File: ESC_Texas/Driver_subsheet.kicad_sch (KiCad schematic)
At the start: 25 parts, among them IC1 UCC21331CQDRQ1, Q1 IPD100N06S4, Q2 IPD100N06S4

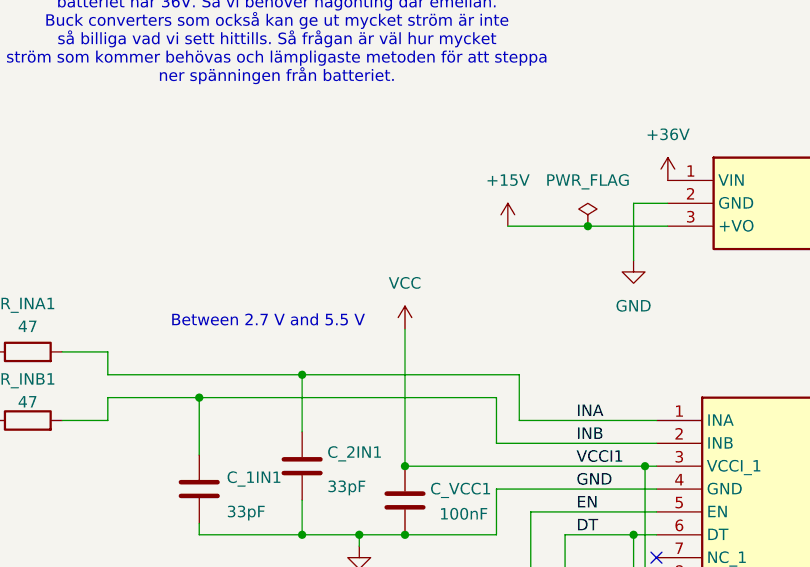
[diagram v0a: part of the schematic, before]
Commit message: Added pin connections
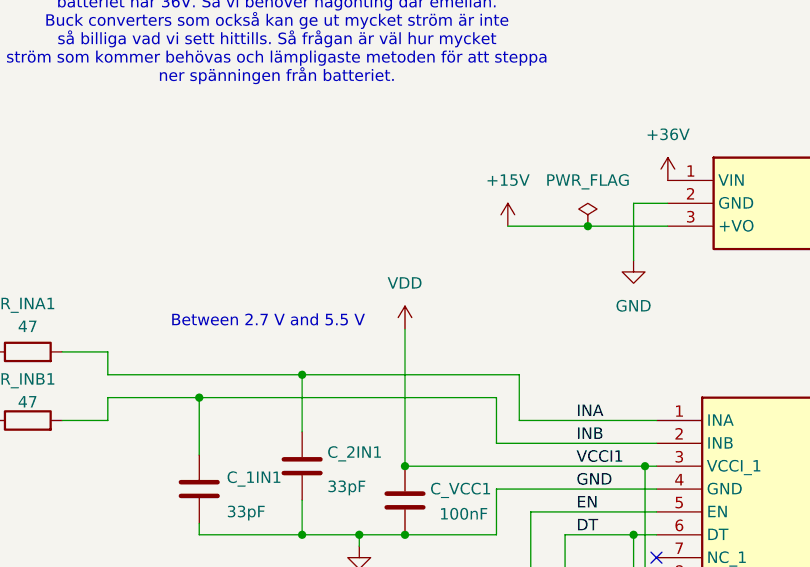
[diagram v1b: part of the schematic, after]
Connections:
- net VCC renamed VDD
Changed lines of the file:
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@@
 			)
 		)
-		(property "Value" "VCC"
+		(property "Value" "VDD"
 			(at 100.33 71.12 0)
 			(effects

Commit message: Started PCB layouting
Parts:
- C_BOOT_A1: value C -> 1uF
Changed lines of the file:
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@@
 			)
 		)
-		(property "Value" "C"
+		(property "Value" "1uF"
 			(at 184.15 96.5199 0)
 			(effects

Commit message: Layout done
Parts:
- removed PS1: MP-K78U15-500R3L, MP-K78U15-500R3L:MPK78U15500R3L, symbol MP-K78U15-500R3L:MP-K78U15-500R3L
- renumbered C_1IN1 to C_1IN2, C_2IN1 to C_2IN2, C_3IN1 to C_3IN2, C_BOOT_A1 to C_BOOT_A2, C_DT1 to C_DT2, C_EN1 to C_EN2, C_VCC1 to C_VCC2, C_VDD_B1 to C_VDD_B2, D1 to D4, D2 to D5, D3 to D6, IC1 to IC7, Q1 to Q3, Q2 to Q4, RR_ON_B1 to RR_ON_B2, R_BOOT_A1 to R_BOOT_A2, R_DT1 to R_DT2, R_GS_A1 to R_GS_A2, R_GS_B1 to R_GS_B2, R_INA1 to R_INA2, R_INB1 to R_INB2, R_OFF_A1 to R_OFF_A2, R_OFF_B1 to R_OFF_B2, R_ON_A1 to R_ON_A2

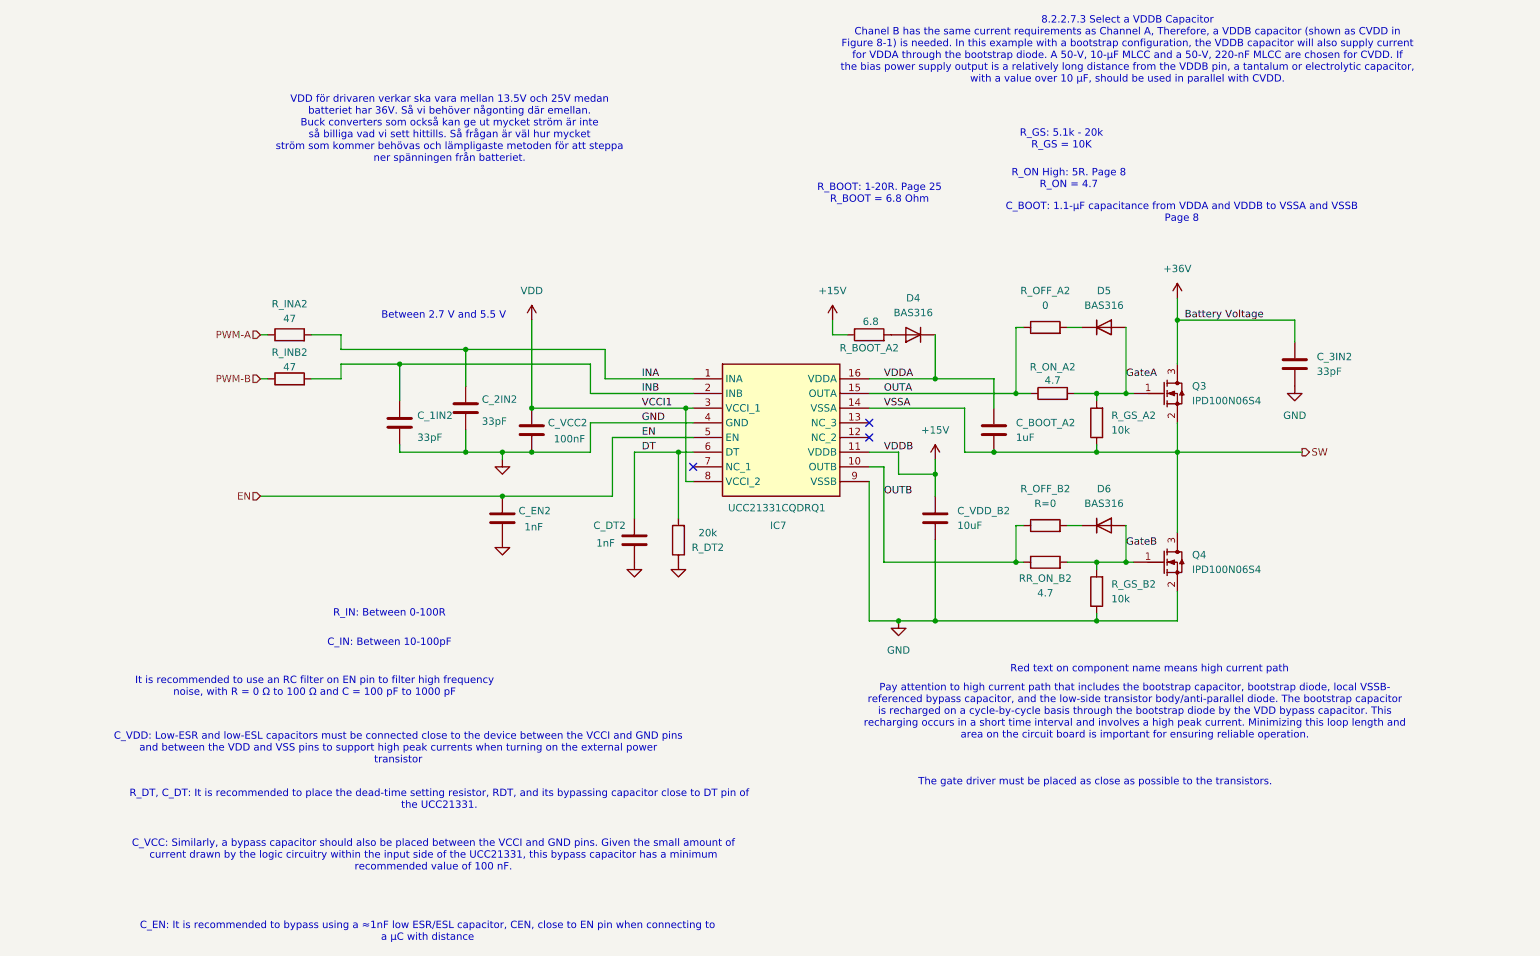
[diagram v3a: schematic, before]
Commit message: Added bypass capacitors to dc/dc...
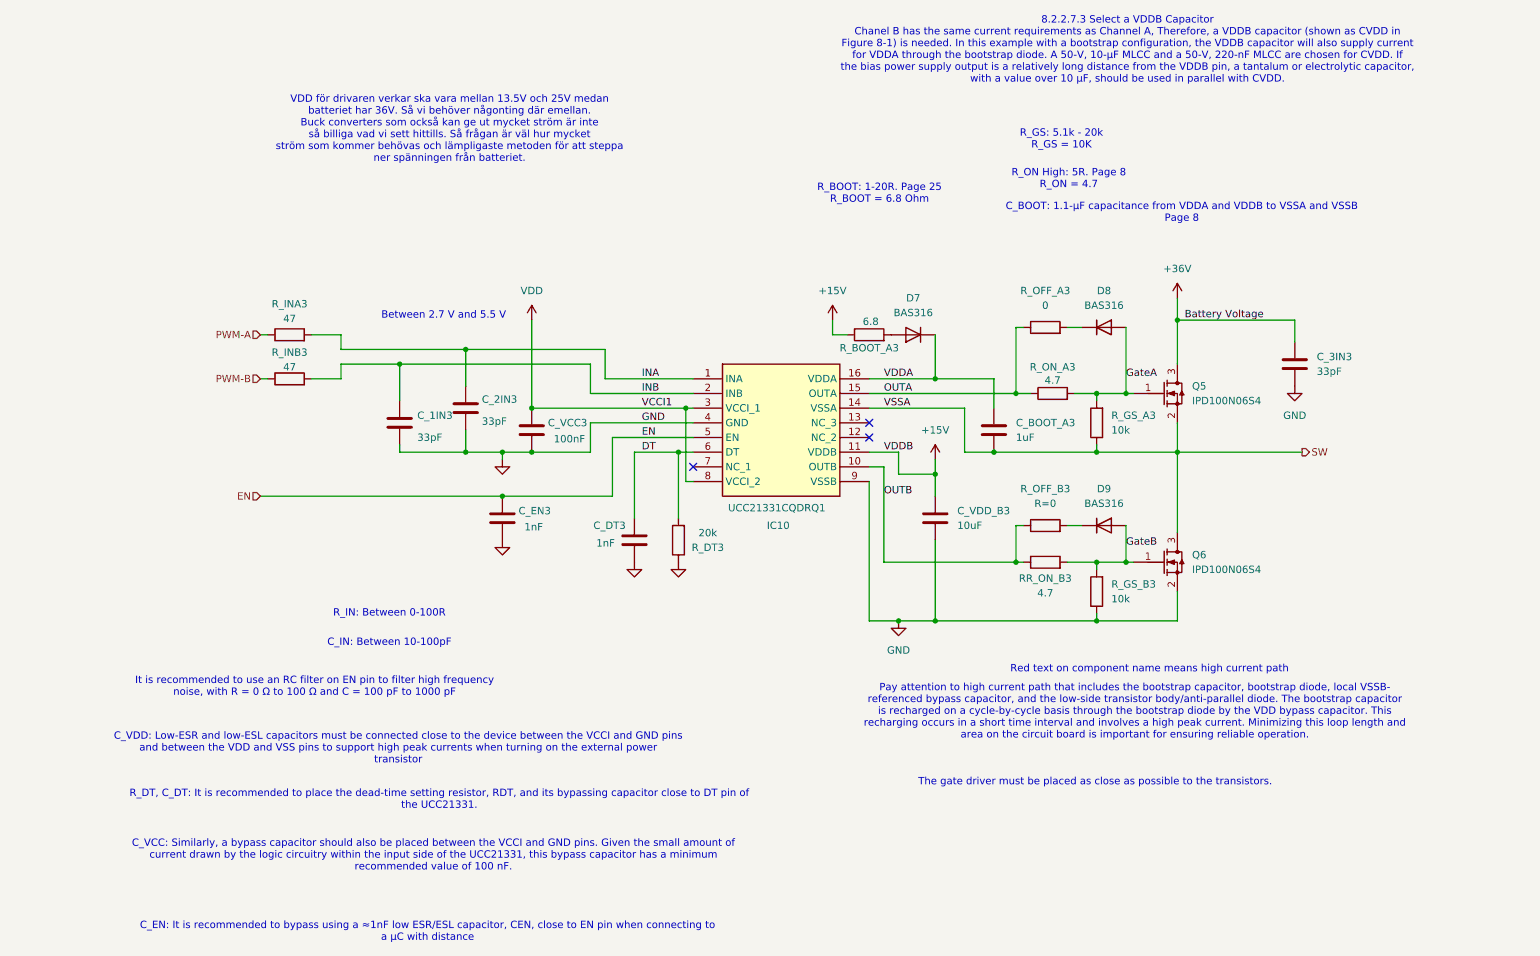
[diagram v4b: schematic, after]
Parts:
- renumbered C_1IN2 to C_1IN3, C_2IN2 to C_2IN3, C_3IN2 to C_3IN3, C_BOOT_A2 to C_BOOT_A3, C_DT2 to C_DT3, C_EN2 to C_EN3, C_VCC2 to C_VCC3, C_VDD_B2 to C_VDD_B3, D4 to D7, D5 to D8, D6 to D9, IC7 to IC10, Q3 to Q5, Q4 to Q6, RR_ON_B2 to RR_ON_B3, R_BOOT_A2 to R_BOOT_A3, R_DT2 to R_DT3, R_GS_A2 to R_GS_A3, R_GS_B2 to R_GS_B3, R_INA2 to R_INA3, R_INB2 to R_INB3, R_OFF_A2 to R_OFF_A3, R_OFF_B2 to R_OFF_B3, R_ON_A2 to R_ON_A3
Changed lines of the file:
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@@
 		(dnp no)
 		(fields_autoplaced yes)
-		(property "Reference" "C_3IN2"
+		(property "Reference" "C_3IN3"
 			(at 236.22 82.5499 0)
 			(effects
@@
 		(on_board yes)
 		(dnp no)
-		(property "Reference" "C_DT2"
+		(property "Reference" "C_DT3"
 			(at 110.998 111.76 0)
 			(effects
@@
 		(on_board yes)
 		(dnp no)
-		(property "Reference" "R_BOOT_A2"
+		(property "Reference" "R_BOOT_A3"
 			(at 158.75 81.026 90)
 			(effects
@@
 		(dnp no)
 		(fields_autoplaced yes)
-		(property "Reference" "#PWR049"
+		(property "Reference" "#PWR068"
 			(at 95.25 120.65 0)
 			(effects
@@
 		(on_board yes)
 		(dnp no)
-		(property "Reference" "R_DT2"
+		(property "Reference" "R_DT3"
 			(at 130.81 115.57 0)
 			(effects
@@
 		(dnp no)
 		(fields_autoplaced yes)
-		(property "Reference" "D6"
+		(property "Reference" "D9"
 			(at 199.39 105.41 0)
 			(effects
@@
 		(on_board yes)
 		(dnp no)
-		(property "Reference" "R_OFF_A2"
+		(property "Reference" "R_OFF_A3"
 			(at 189.23 71.12 90)
 			(effects
@@
 		(dnp no)
 		(fields_autoplaced yes)
-		(property "Reference" "#PWR048"
+		(property "Reference" "#PWR067"
 			(at 95.25 106.68 0)
 			(effects
@@
 		(on_board yes)
 		(dnp no)
-		(property "Reference" "C_VDD_B2"
+		(property "Reference" "C_VDD_B3"
 			(at 173.99 109.2199 0)
 			(effects
@@
 		(on_board yes)
 		(dnp no)
-		(property "Reference" "RR_ON_B2"
+		(property "Reference" "RR_ON_B3"
 			(at 189.23 120.904 90)
 			(effects
@@
 		(on_board yes)
 		(dnp no)
-		(property "Reference" "R_GS_B2"
+		(property "Reference" "R_GS_B3"
 			(at 200.66 121.9199 0)
 			(effects
@@
 		(dnp no)
 		(fields_autoplaced yes)
-		(property "Reference" "#PWR052"
+		(property "Reference" "#PWR071"
 			(at 125.73 124.46 0)
 			(effects
@@
 		(dnp no)
 		(fields_autoplaced yes)
-		(property "Reference" "#PWR057"
+		(property "Reference" "#PWR076"
 			(at 232.41 93.98 0)
 			(effects
@@
 		(dnp no)
 		(fields_autoplaced yes)
-		(property "Reference" "#PWR050"
+		(property "Reference" "#PWR069"
 			(at 100.33 80.01 0)
 			(effects
@@
 		(dnp no)
 		(fields_autoplaced yes)
-		(property "Reference" "R_OFF_B2"
+		(property "Reference" "R_OFF_B3"
 			(at 189.23 105.41 90)
 			(effects
@@
 		(dnp no)
 		(fields_autoplaced yes)
-		(property "Reference" "D5"
+		(property "Reference" "D8"
 			(at 199.39 71.12 0)
 			(effects
@@
 		(dnp no)
 		(fields_autoplaced yes)
-		(property "Reference" "#PWR056"
+		(property "Reference" "#PWR075"
 			(at 212.09 76.2 0)
 			(effects
@@
 		(dnp no)
 		(fields_autoplaced yes)
-		(property "Reference" "Q4"
+		(property "Reference" "Q6"
 			(at 214.63 116.8399 0)
 			(effects
@@
 		(on_board yes)
 		(dnp no)
-		(property "Reference" "C_VCC2"
+		(property "Reference" "C_VCC3"
 			(at 103.124 93.98 0)
 			(effects
@@
 		(on_board yes)
 		(dnp no)
-		(property "Reference" "C_1IN2"
+		(property "Reference" "C_1IN3"
 			(at 80.518 92.71 0)
 			(effects
@@
 		(dnp no)
 		(fields_autoplaced yes)
-		(property "Reference" "#PWR051"
+		(property "Reference" "#PWR070"
 			(at 118.11 124.46 0)
 			(effects
@@
 		(dnp no)
 		(fields_autoplaced yes)
-		(property "Reference" "R_GS_A2"
+		(property "Reference" "R_GS_A3"
 			(at 200.66 92.7099 0)
 			(effects
@@
 		(on_board yes)
 		(dnp no)
-		(property "Reference" "R_INA2"
+		(property "Reference" "R_INA3"
 			(at 58.42 73.406 90)
 			(effects
@@
 		(on_board yes)
 		(dnp no)
-		(property "Reference" "C_EN2"
+		(property "Reference" "C_EN3"
 			(at 98.044 109.22 0)
 			(effects
@@
 		(dnp no)
 		(fields_autoplaced yes)
-		(property "Reference" "#PWR055"
+		(property "Reference" "#PWR074"
 			(at 170.18 104.14 0)
 			(effects
@@
 		(on_board yes)
 		(dnp no)
-		(property "Reference" "R_INB2"
+		(property "Reference" "R_INB3"
 			(at 58.42 81.788 90)
 			(effects
@@
 		(dnp no)
 		(fields_autoplaced yes)
-		(property "Reference" "D4"
+		(property "Reference" "D7"
 			(at 166.37 72.39 0)
 			(effects
@@
 		(on_board yes)
 		(dnp no)
-		(property "Reference" "IC7"
+		(property "Reference" "IC10"
 			(at 143.002 111.76 0)
 			(effects
@@
 		(on_board yes)
 		(dnp no)
-		(property "Reference" "R_ON_A2"
+		(property "Reference" "R_ON_A3"
 			(at 190.5 84.328 90)
 			(effects
@@
 		(dnp no)
 		(fields_autoplaced yes)
-		(property "Reference" "#PWR054"
+		(property "Reference" "#PWR073"
 			(at 163.83 134.62 0)
 			(effects
@@
 		(on_board yes)
 		(dnp no)
-		(property "Reference" "C_2IN2"
+		(property "Reference" "C_2IN3"
 			(at 91.694 89.916 0)
 			(effects
@@
 		(on_board yes)
 		(dnp no)
-		(property "Reference" "C_BOOT_A2"
+		(property "Reference" "C_BOOT_A3"
 			(at 184.15 93.9799 0)
 			(effects
@@
 		(dnp no)
 		(fields_autoplaced yes)
-		(property "Reference" "#PWR053"
+		(property "Reference" "#PWR072"
 			(at 152.4 80.01 0)
 			(effects
@@
 		(dnp no)
 		(fields_autoplaced yes)
-		(property "Reference" "Q3"
+		(property "Reference" "Q5"
 			(at 214.63 87.6299 0)
 			(effects

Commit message: Started new additions
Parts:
- removed Q6: IPD100N06S4, IPD100N06S4-03:TRANS_BTS3060TFATMA1, symbol Transistor_FET:BSP129
- added Q2: IPD100N06S4, IPD100N06S4-03:TRANS_BTS3060TFATMA1, symbol Transistor_FET:BSP129
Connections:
- net +36V: now also Q5.2 (D); no longer Q5.3 (D)
- net GND: now also Q2.3 (S)
- net GateB: now also Q2.1 (G)
- net SW: now also Q5.3 (S), Q2.2 (D); no longer Q5.2 (S)
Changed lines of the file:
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@@
+	)
+	(symbol
+		(lib_name "BSP129_1")
+		(lib_id "Transistor_FET:BSP129")
+		(at 209.55 118.11 0)
+		(unit 1)
+		(exclude_from_sim no)
+		(in_bom yes)
+		(on_board yes)
+		(dnp no)
+		(fields_autoplaced yes)
+		(property "Reference" "Q2"
+			(at 214.63 116.8399 0)
+			(effects
+				(font
+					(size 1.27 1.27)
+				)
+				(justify left)
+			)
+		)
+		(property "Value" "IPD100N06S4"
+			(at 214.63 119.3799 0)
+			(effects
+				(font
+					(size 1.27 1.27)
+				)
+				(justify left)
+			)
+		)
+		(property "Footprint" "IPD100N06S4-03:TRANS_BTS3060TFATMA1"
+			(at 214.122 133.223 0)
+			(effects
+				(font
+					(size 1.27 1.27)
+					(italic yes)
+				)
+				(justify left)
+				(hide yes)
+			)
+		)
+		(property "Datasheet" "https://www.infineon.com/dgdl/Infineon-BSP129-DS-v01_42-en.pdf?fileId=db3a30433c1a8752013c1fc296d2395f"
+			(at 214.122 135.128 0)
+			(effects
+				(font
+					(size 1.27 1.27)
+				)
+				(justify left)
+				(hide yes)
+			)
+		)
+		(property "Description" "0.35A Id, 240V Vds, N-Channel MOSFET, SOT-223"
+			(at 209.042 131.318 0)
+			(effects
+				(font
+					(size 1.27 1.27)
+				)
+				(hide yes)
+			)
+		)
+		(pin "1"
+		)
+		(pin "2"
+		)
+		(pin "3"
+		)
+		(instances
+			(project "ESC_Texas"
+				(path "/0e3a5351-d2cd-4ecc-a1be-cca9c5f62ea0/553690e4-0a20-4b8e-821c-55ba3788d3c5/2b378908-a00b-4e0f-9184-1d2f8bdf9466"
+					(reference "Q6")
+					(unit 1)
+				)
+				(path "/0e3a5351-d2cd-4ecc-a1be-cca9c5f62ea0/63c8dce8-451d-41ee-b438-d688cf3e64bd/2b378908-a00b-4e0f-9184-1d2f8bdf9466"
+					(reference "Q4")
+					(unit 1)
+				)
+				(path "/0e3a5351-d2cd-4ecc-a1be-cca9c5f62ea0/b8e552f6-93a8-4098-a907-a65be165d984/2b378908-a00b-4e0f-9184-1d2f8bdf9466"
+					(reference "Q2")
+					(unit 1)
+				)
+			)
+		)
 	)
 	(symbol
@@
 	)
 	(symbol
-		(lib_name "BSP129_2")
-		(lib_id "Transistor_FET:BSP129")
-		(at 209.55 118.11 0)
-		(unit 1)
-		(exclude_from_sim no)
-		(in_bom yes)
-		(on_board yes)
-		(dnp no)
-		(fields_autoplaced yes)
-		(property "Reference" "Q6"
-			(at 214.63 116.8399 0)
-			(effects
-				(font
-					(size 1.27 1.27)
-				)
-				(justify left)
-			)
-		)
-		(property "Value" "IPD100N06S4"
-			(at 214.63 119.3799 0)
-			(effects
-				(font
-					(size 1.27 1.27)
-				)
-				(justify left)
-			)
-		)
-		(property "Footprint" "IPD100N06S4-03:TRANS_BTS3060TFATMA1"
-			(at 214.122 133.223 0)
-			(effects
-				(font
-					(size 1.27 1.27)
-					(italic yes)
-				)
-				(justify left)
-				(hide yes)
-			)
-		)
-		(property "Datasheet" "https://www.infineon.com/dgdl/Infineon-BSP129-DS-v01_42-en.pdf?fileId=db3a30433c1a8752013c1fc296d2395f"
-			(at 214.122 135.128 0)
-			(effects
-				(font
-					(size 1.27 1.27)
-				)
-				(justify left)
-				(hide yes)
-			)
-		)
-		(property "Description" "0.35A Id, 240V Vds, N-Channel MOSFET, SOT-223"
-			(at 209.042 131.318 0)
-			(effects
-				(font
-					(size 1.27 1.27)
-				)
-				(hide yes)
-			)
-		)
-		(pin "1"
-		)
-		(pin "2"
-		)
-		(pin "3"
-		)
-		(instances
-			(project "ESC_Texas"
-				(path "/0e3a5351-d2cd-4ecc-a1be-cca9c5f62ea0/553690e4-0a20-4b8e-821c-55ba3788d3c5/2b378908-a00b-4e0f-9184-1d2f8bdf9466"
-					(reference "Q6")
-					(unit 1)
-				)
-				(path "/0e3a5351-d2cd-4ecc-a1be-cca9c5f62ea0/63c8dce8-451d-41ee-b438-d688cf3e64bd/2b378908-a00b-4e0f-9184-1d2f8bdf9466"
-					(reference "Q4")
-					(unit 1)
-				)
-				(path "/0e3a5351-d2cd-4ecc-a1be-cca9c5f62ea0/b8e552f6-93a8-4098-a907-a65be165d984/2b378908-a00b-4e0f-9184-1d2f8bdf9466"
-					(reference "Q2")
-					(unit 1)
-				)
-			)
-		)
-	)
-	(symbol
 		(lib_id "Device:C")
 		(at 100.33 95.25 0)
@@
 	)
 	(symbol
-		(lib_name "BSP129_2")
+		(lib_name "BSP129_1")
 		(lib_id "Transistor_FET:BSP129")
 		(at 209.55 88.9 0)
